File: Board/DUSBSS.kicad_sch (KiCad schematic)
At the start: 5 parts, among them J2 USB_C_Receptacle_USB2.0_16P, J3 USB_C_Receptacle_USB2.0_16P, U5 AP22652W6-7, U6 INA226, U7 INA226

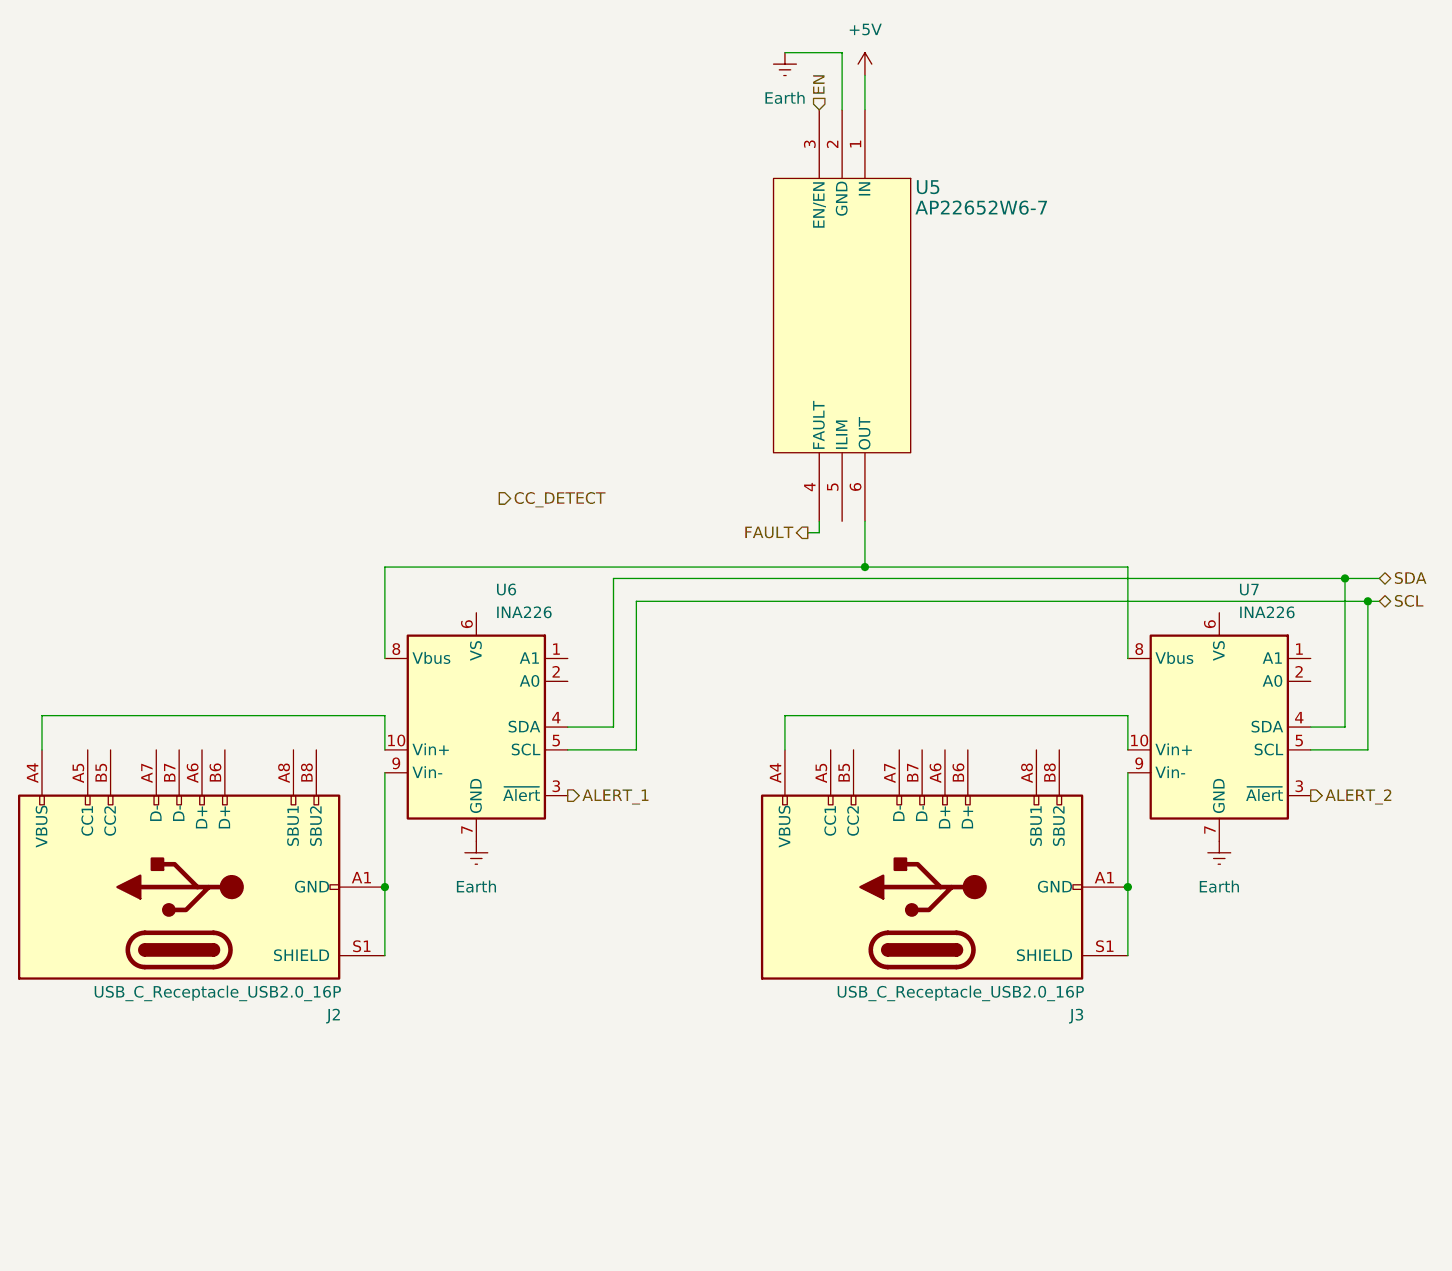
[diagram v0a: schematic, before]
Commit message: New Layout and power
Made power for 3v3
all usb added
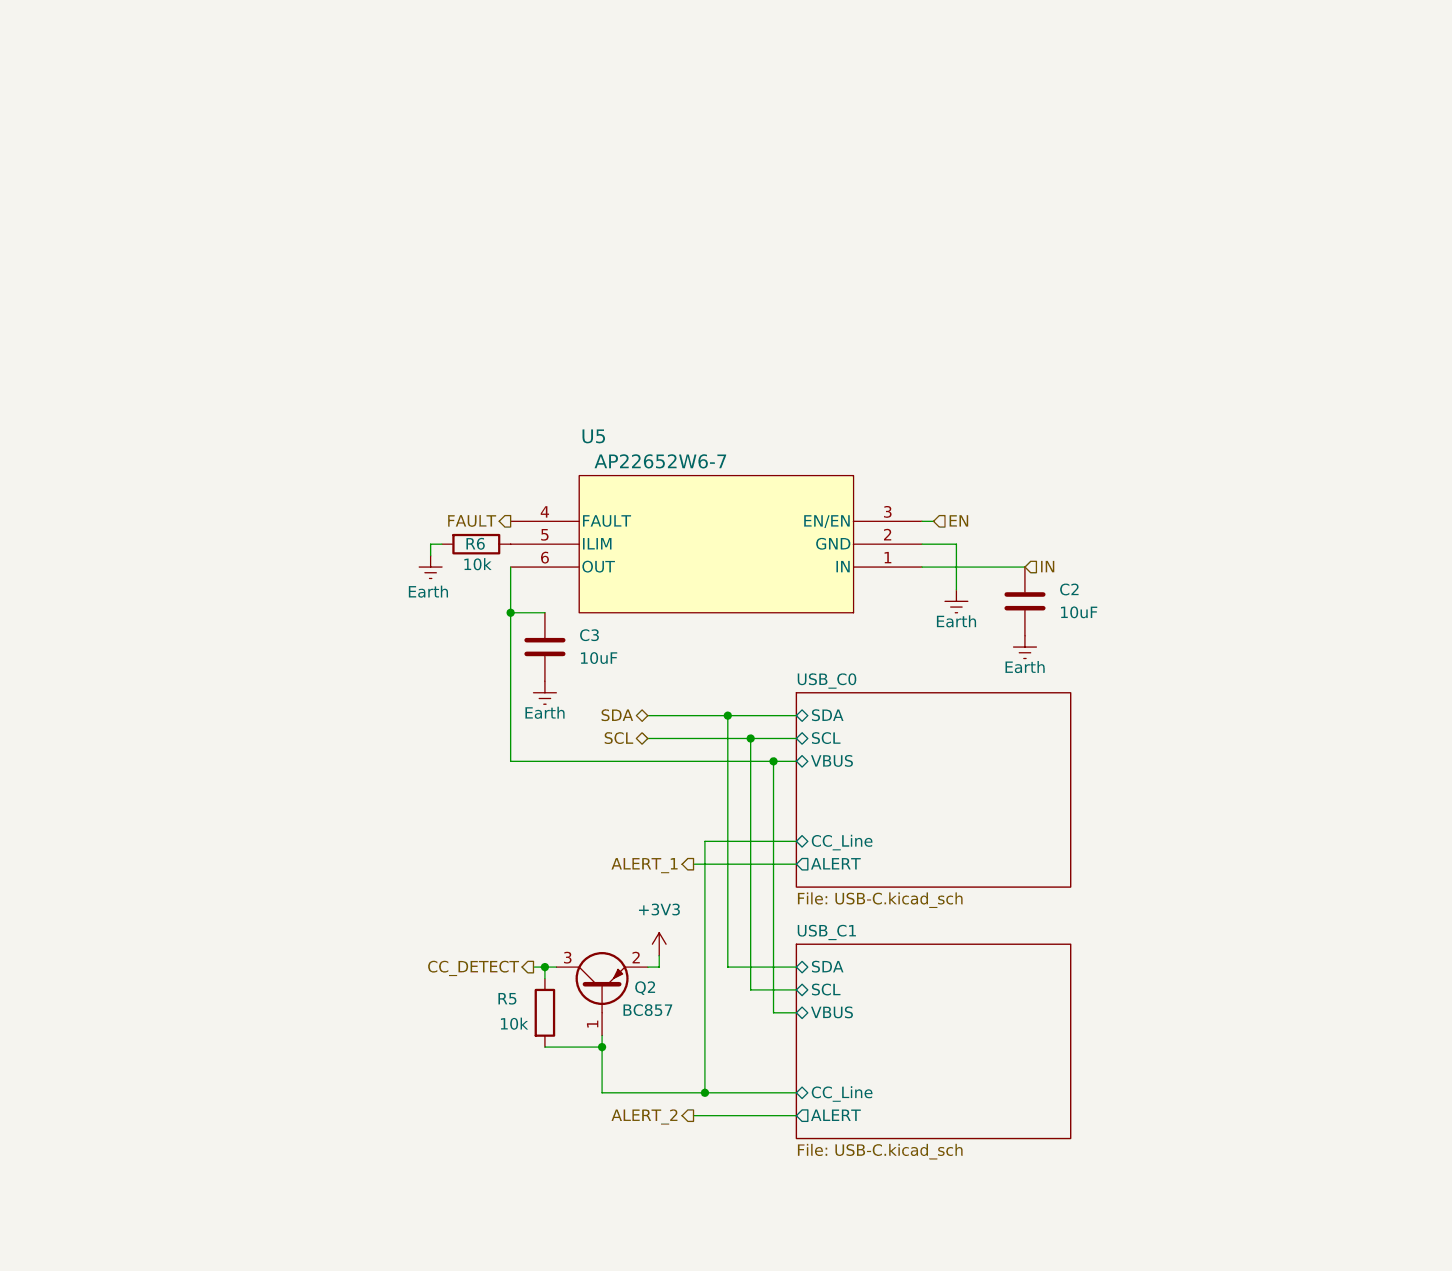
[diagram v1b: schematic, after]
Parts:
- removed J2, J3: USB_C_Receptacle_USB2.0_16P, symbol Connector:USB_C_Receptacle_USB2.0_16P
- removed U6, U7: INA226, Package_SO:VSSOP-10_3x3mm_P0.5mm, symbol Sensor_Energy:INA226
- added C2, C3: 10uF, symbol Device:C
- added Q2: BC857, Package_TO_SOT_SMD:SOT-23, symbol Transistor_BJT:BC857
- added R5, R6: 10k, symbol Device:R
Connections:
- net CC_DETECT: now also Q2.3 (C), R5.1
- net Earth: now also C2.2, C3.2, R6.2
- net USB_C0/VBUS: now reaches U5.6 (OUT)
- net USB_C0/VBUS: now also C3.1
- net at U5.5 (ILIM): now also R6.1
- net +5V renamed IN
- net IN: now also C2.1
- new net +3V3: Q2.2 (E)
- new net USB_C0/CC_Line: Q2.1 (B), R5.2
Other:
- added sheet USB_C0 (USB-C.kicad_sch)
- added sheet USB_C1 (USB-C.kicad_sch)
- moved on the sheet: U5

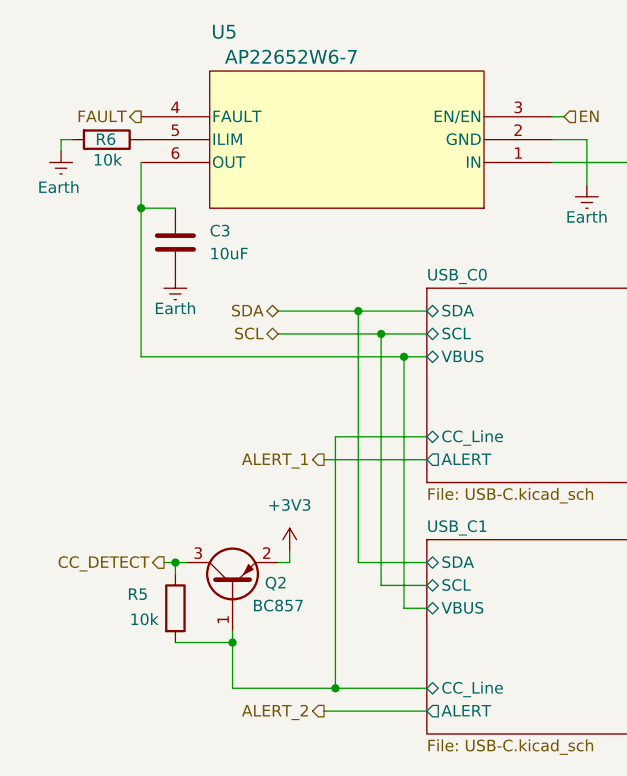
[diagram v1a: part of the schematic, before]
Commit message: Saving pins
-4 pins to connect to gpio thanks for ability to use two or more alert pins on one gpio
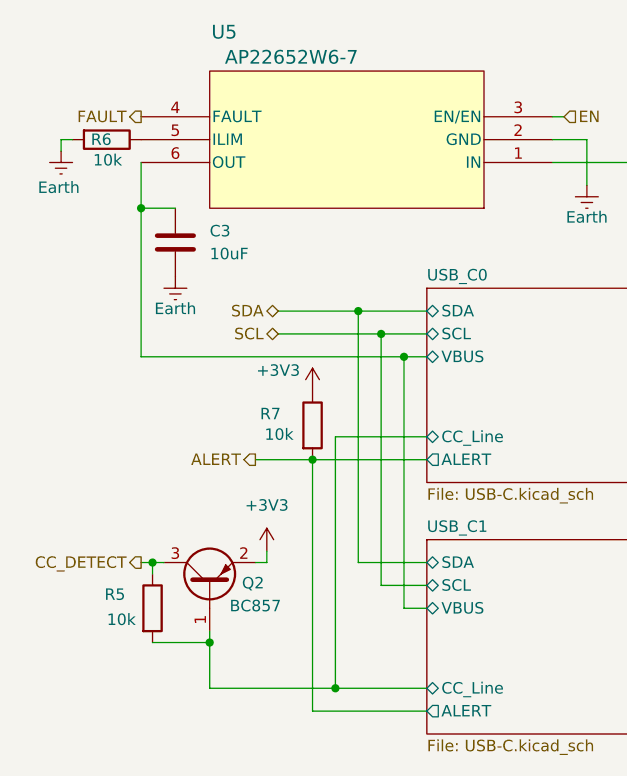
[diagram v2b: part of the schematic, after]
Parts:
- added R7: 10k, symbol Device:R
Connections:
- net +3V3: now also R7.1
- new net ALERT: R7.2
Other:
- moved on the sheet: Q2, R5

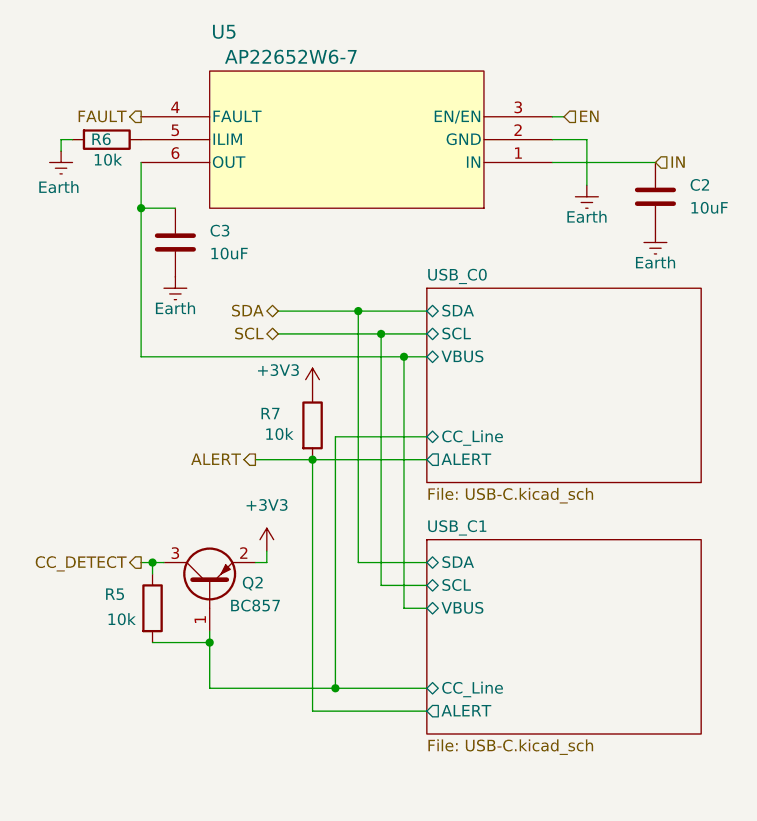
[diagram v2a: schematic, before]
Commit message: Conecting usb to esp
added in/out and out/in reistry
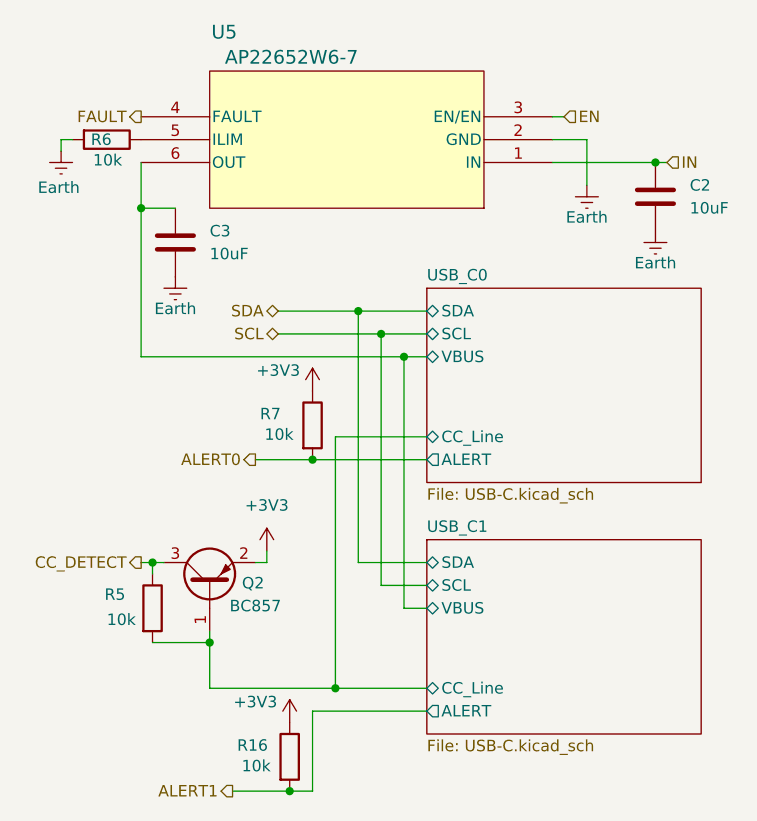
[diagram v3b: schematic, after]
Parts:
- added R16: 10k, symbol Device:R
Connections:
- net +3V3: now also R16.1
- net ALERT renamed ALERT0
- new net ALERT1: R16.2
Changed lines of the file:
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@@
+	)
+	(junction
+		(at 181.61 81.28)
+		(diameter 0)
+		(color 0 0 0 0)
 	)
 	(junction
@@
 	)
 	(junction
+		(at 140.97 151.13)
+		(diameter 0)
+		(color 0 0 0 0)
+	)
+	(junction
 		(at 143.51 114.3)
 		(diameter 0)
@@
 	(wire
 		(pts
+			(xy 143.51 142.24) (xy 143.51 151.13)
+		)
+		(stroke
+			(width 0)
+			(type default)
+		)
+	)
+	(wire
+		(pts
 			(xy 132.08 139.7) (xy 146.05 139.7)
 		)
@@
 	(wire
 		(pts
+			(xy 140.97 151.13) (xy 134.62 151.13)
+		)
+		(stroke
+			(width 0)
+			(type default)
+		)
+	)
+	(wire
+		(pts
 			(xy 128.27 86.36) (xy 124.46 86.36)
 		)
@@
 	(wire
 		(pts
+			(xy 143.51 151.13) (xy 140.97 151.13)
+		)
+		(stroke
+			(width 0)
+			(type default)
+		)
+	)
+	(wire
+		(pts
 			(xy 138.43 125.73) (xy 137.16 125.73)
 		)
@@
 	(wire
 		(pts
-			(xy 143.51 114.3) (xy 143.51 142.24)
-		)
-		(stroke
-			(width 0)
-			(type default)
-		)
-	)
-	(wire
-		(pts
 			(xy 146.05 111.76) (xy 156.21 111.76)
 		)
@@
 		(pts
 			(xy 125.73 134.62) (xy 132.08 134.62)
+		)
+		(stroke
+			(width 0)
+			(type default)
+		)
+	)
+	(wire
+		(pts
+			(xy 182.88 81.28) (xy 181.61 81.28)
 		)
 		(stroke
@@
 	(hierarchical_label "IN"
 		(shape input)
-		(at 181.61 81.28 0)
+		(at 182.88 81.28 0)
 		(effects
 			(font
@@
 		)
 	)
-	(hierarchical_label "ALERT"
+	(hierarchical_label "ALERT0"
 		(shape output)
 		(at 137.16 114.3 180)
@@
 			)
 			(justify right)
+		)
+	)
+	(hierarchical_label "ALERT1"
+		(shape output)
+		(at 134.62 151.13 180)
+		(effects
+			(font
+				(size 1.27 1.27)
+			)
+			(justify right)
+		)
+	)
+	(symbol
+		(lib_id "power:+3V3")
+		(at 140.97 143.51 0)
+		(unit 1)
+		(exclude_from_sim no)
+		(in_bom yes)
+		(on_board yes)
+		(dnp no)
+		(property "Reference" "#PWR020"
+			(at 140.97 147.32 0)
+			(effects
+				(font
+					(size 1.27 1.27)
+				)
+				(hide yes)
+			)
+		)
+		(property "Value" "+3V3"
+			(at 137.16 141.224 0)
+			(effects
+				(font
+					(size 1.27 1.27)
+				)
+			)
+		)
+		(property "Footprint" ""
+			(at 140.97 143.51 0)
+			(effects
+				(font
+					(size 1.27 1.27)
+				)
+				(hide yes)
+			)
+		)
+		(property "Datasheet" ""
+			(at 140.97 143.51 0)
+			(effects
+				(font
+					(size 1.27 1.27)
+				)
+				(hide yes)
+			)
+		)
+		(property "Description" "Power symbol creates a global label with name \"+3V3\""
+			(at 140.97 143.51 0)
+			(effects
+				(font
+					(size 1.27 1.27)
+				)
+				(hide yes)
+			)
+		)
+		(pin "1"
+		)
+		(instances
+			(project "SlimeVR_Dock"
+				(path "/06ff9557-1f9b-4670-8a34-bb7684a016dd/20608bd6-1177-4976-ba2c-965ba6250d58"
+					(reference "#PWR020")
+					(unit 1)
+				)
+				(path "/06ff9557-1f9b-4670-8a34-bb7684a016dd/21559adc-22f0-4da5-bb39-da22b4a6076e"
+					(reference "#PWR049")
+					(unit 1)
+				)
+				(path "/06ff9557-1f9b-4670-8a34-bb7684a016dd/2b86b0ae-2209-4a30-98e5-d26e75080e9f"
+					(reference "#PWR050")
+					(unit 1)
+				)
+				(path "/06ff9557-1f9b-4670-8a34-bb7684a016dd/c6b53444-adaa-455c-990e-02e7d6acd668"
+					(reference "#PWR048")
+					(unit 1)
+				)
+			)
 		)
 	)
@@
 	)
 	(symbol
+		(lib_id "Device:R")
+		(at 140.97 147.32 0)
+		(unit 1)
+		(exclude_from_sim no)
+		(in_bom yes)
+		(on_board yes)
+		(dnp no)
+		(property "Reference" "R16"
+			(at 135.128 146.05 0)
+			(effects
+				(font
+					(size 1.27 1.27)
+				)
+				(justify left)
+			)
+		)
+		(property "Value" "10k"
+			(at 135.636 148.336 0)
+			(effects
+				(font
+					(size 1.27 1.27)
+				)
+				(justify left)
+			)
+		)
+		(property "Footprint" ""
+			(at 139.192 147.32 90)
+			(effects
+				(font
+					(size 1.27 1.27)
+				)
+				(hide yes)
+			)
+		)
+		(property "Datasheet" "~"
+			(at 140.97 147.32 0)
+			(effects
+				(font
+					(size 1.27 1.27)
+				)
+				(hide yes)
+			)
+		)
+		(property "Description" "Resistor"
+			(at 140.97 147.32 0)
+			(effects
+				(font
+					(size 1.27 1.27)
+				)
+				(hide yes)
+			)
+		)
+		(pin "1"
+		)
+		(pin "2"
+		)
+		(instances
+			(project "SlimeVR_Dock"
+				(path "/06ff9557-1f9b-4670-8a34-bb7684a016dd/20608bd6-1177-4976-ba2c-965ba6250d58"
+					(reference "R16")
+					(unit 1)
+				)
+				(path "/06ff9557-1f9b-4670-8a34-bb7684a016dd/21559adc-22f0-4da5-bb39-da22b4a6076e"
+					(reference "R18")
+					(unit 1)
+				)
+				(path "/06ff9557-1f9b-4670-8a34-bb7684a016dd/2b86b0ae-2209-4a30-98e5-d26e75080e9f"
+					(reference "R19")
+					(unit 1)
+				)
+				(path "/06ff9557-1f9b-4670-8a34-bb7684a016dd/c6b53444-adaa-455c-990e-02e7d6acd668"
+					(reference "R17")
+					(unit 1)
+				)
+			)
+		)
+	)
+	(symbol
 		(lib_id "Library:AP22652W6-7")
 		(at 170.18 81.28 180)
@@
 		)
 	)
-	(sheet_instances
-		(path "/"
-			(page "1")
-		)
-	)
-	(embedded_fonts no)
 )
